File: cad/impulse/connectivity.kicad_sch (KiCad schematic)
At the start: 45 parts, among them J13 Micro_SD_Card, J14 Conn_Coaxial, U11 W25Q32JVSS, U12 BGS12PL6, U13 SX1268, Y2 XL7EL89COI-111YLC-32M

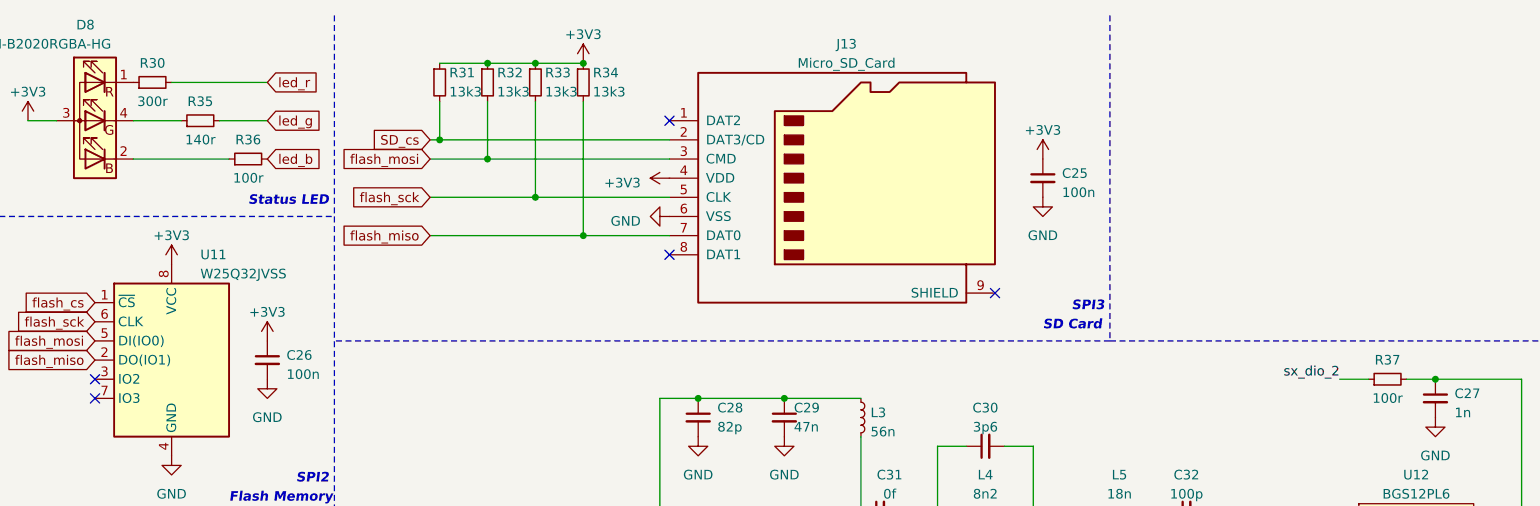
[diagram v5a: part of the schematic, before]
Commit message: Modified oscillator circuit.
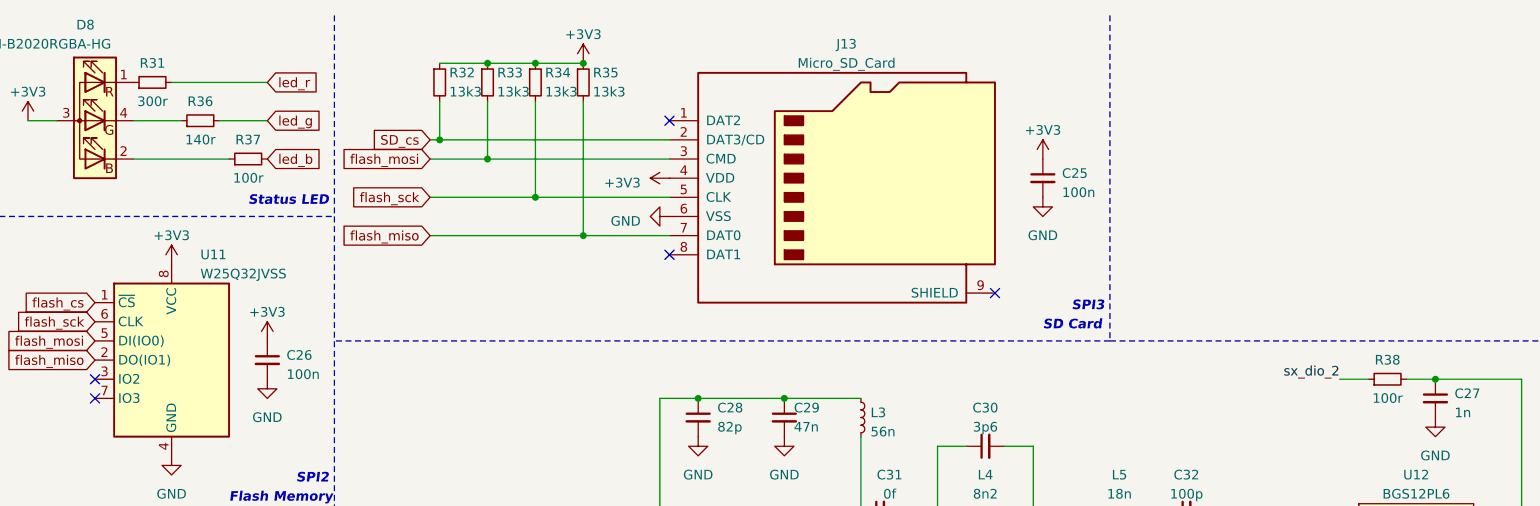
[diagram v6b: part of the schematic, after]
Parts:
- renumbered R30 to R31, R31 to R32, R32 to R33, R33 to R34, R34 to R35, R35 to R36, R36 to R37, R37 to R38
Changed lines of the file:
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@@
   (symbol (lib_id "Device:R_Small") (at 52.07 31.75 90) (unit 1)
     (in_bom yes) (on_board yes) (dnp no)
-    (property "Reference" "R36" (at 52.07 29.21 90)
+    (property "Reference" "R37" (at 52.07 29.21 90)
       (effects (font (size 1.27 1.27)))
     )
@@
       (project "impulse"
         (path "/eb4cfece-5fcb-437a-ac58-337ab6512039/b32decc0-dca7-4695-ab8c-927869a0cdf3"
-          (reference "R36") (unit 1)
+          (reference "R37") (unit 1)
         )
       )
@@
   (symbol (lib_id "Device:R_Small") (at 77.47 21.59 0) (unit 1)
     (in_bom yes) (on_board yes) (dnp no)
-    (property "Reference" "R31" (at 78.74 20.32 0)
+    (property "Reference" "R32" (at 78.74 20.32 0)
       (effects (font (size 1.27 1.27)) (justify left))
     )
@@
       (project "impulse"
         (path "/eb4cfece-5fcb-437a-ac58-337ab6512039/b32decc0-dca7-4695-ab8c-927869a0cdf3"
-          (reference "R31") (unit 1)
+          (reference "R32") (unit 1)
         )
       )
@@
   (symbol (lib_id "Device:R_Small") (at 45.72 26.67 90) (unit 1)
     (in_bom yes) (on_board yes) (dnp no)
-    (property "Reference" "R35" (at 45.72 24.13 90)
+    (property "Reference" "R36" (at 45.72 24.13 90)
       (effects (font (size 1.27 1.27)))
     )
@@
       (project "impulse"
         (path "/eb4cfece-5fcb-437a-ac58-337ab6512039/b32decc0-dca7-4695-ab8c-927869a0cdf3"
-          (reference "R35") (unit 1)
+          (reference "R36") (unit 1)
         )
       )
@@
   (symbol (lib_id "Device:R_Small") (at 203.2 60.96 90) (unit 1)
     (in_bom yes) (on_board yes) (dnp no)
-    (property "Reference" "R37" (at 203.2 58.42 90)
+    (property "Reference" "R38" (at 203.2 58.42 90)
       (effects (font (size 1.27 1.27)))
     )
@@
       (project "impulse"
         (path "/eb4cfece-5fcb-437a-ac58-337ab6512039/b32decc0-dca7-4695-ab8c-927869a0cdf3"
-          (reference "R37") (unit 1)
+          (reference "R38") (unit 1)
         )
       )
@@
   (symbol (lib_id "Device:R_Small") (at 90.17 21.59 0) (unit 1)
     (in_bom yes) (on_board yes) (dnp no)
-    (property "Reference" "R33" (at 91.44 20.32 0)
+    (property "Reference" "R34" (at 91.44 20.32 0)
       (effects (font (size 1.27 1.27)) (justify left))
     )
@@
       (project "impulse"
         (path "/eb4cfece-5fcb-437a-ac58-337ab6512039/b32decc0-dca7-4695-ab8c-927869a0cdf3"
+          (reference "R34") (unit 1)
+        )
+      )
+    )
+  )
+  (symbol (lib_id "Device:R_Small") (at 83.82 21.59 0) (unit 1)
+    (in_bom yes) (on_board yes) (dnp no)
+    (property "Reference" "R33" (at 85.09 20.32 0)
+      (effects (font (size 1.27 1.27)) (justify left))
+    )
+    (property "Value" "13k3" (at 85.09 22.86 0)
+      (effects (font (size 1.27 1.27)) (justify left))
+    )
+    (property "Footprint" "Resistor_SMD:R_0402_1005Metric" (at 83.82 21.59 0)
+      (effects (font (size 1.27 1.27)) hide)
+    )
+    (property "Datasheet" "~" (at 83.82 21.59 0)
+      (effects (font (size 1.27 1.27)) hide)
+    )
+    (property "lcsc" "C3015832" (at 83.82 21.59 0)
+      (effects (font (size 1.27 1.27)) hide)
+    )
+    (pin "1")
+    (pin "2")
+    (instances
+      (project "impulse"
+        (path "/eb4cfece-5fcb-437a-ac58-337ab6512039/b32decc0-dca7-4695-ab8c-927869a0cdf3"
           (reference "R33") (unit 1)
-        )
-      )
-    )
-  )
-  (symbol (lib_id "Device:R_Small") (at 83.82 21.59 0) (unit 1)
-    (in_bom yes) (on_board yes) (dnp no)
-    (property "Reference" "R32" (at 85.09 20.32 0)
-      (effects (font (size 1.27 1.27)) (justify left))
-    )
-    (property "Value" "13k3" (at 85.09 22.86 0)
-      (effects (font (size 1.27 1.27)) (justify left))
-    )
-    (property "Footprint" "Resistor_SMD:R_0402_1005Metric" (at 83.82 21.59 0)
-      (effects (font (size 1.27 1.27)) hide)
-    )
-    (property "Datasheet" "~" (at 83.82 21.59 0)
-      (effects (font (size 1.27 1.27)) hide)
-    )
-    (property "lcsc" "C3015832" (at 83.82 21.59 0)
-      (effects (font (size 1.27 1.27)) hide)
-    )
-    (pin "1")
-    (pin "2")
-    (instances
-      (project "impulse"
-        (path "/eb4cfece-5fcb-437a-ac58-337ab6512039/b32decc0-dca7-4695-ab8c-927869a0cdf3"
-          (reference "R32") (unit 1)
         )
       )
@@
   (symbol (lib_id "Device:R_Small") (at 96.52 21.59 0) (unit 1)
     (in_bom yes) (on_board yes) (dnp no)
-    (property "Reference" "R34" (at 97.79 20.32 0)
+    (property "Reference" "R35" (at 97.79 20.32 0)
       (effects (font (size 1.27 1.27)) (justify left))
     )
@@
       (project "impulse"
         (path "/eb4cfece-5fcb-437a-ac58-337ab6512039/b32decc0-dca7-4695-ab8c-927869a0cdf3"
-          (reference "R34") (unit 1)
+          (reference "R35") (unit 1)
         )
       )
@@
   (symbol (lib_id "Device:R_Small") (at 39.37 21.59 90) (unit 1)
     (in_bom yes) (on_board yes) (dnp no)
-    (property "Reference" "R30" (at 39.37 19.05 90)
+    (property "Reference" "R31" (at 39.37 19.05 90)
       (effects (font (size 1.27 1.27)))
     )
@@
       (project "impulse"
         (path "/eb4cfece-5fcb-437a-ac58-337ab6512039/b32decc0-dca7-4695-ab8c-927869a0cdf3"
-          (reference "R30") (unit 1)
-        )
-      )
+          (reference "R31") (unit 1)
+        )
+      )

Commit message: First layout.
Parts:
- renumbered R31 to R32, R32 to R33, R33 to R34, R34 to R35, R35 to R36, R36 to R37, R37 to R38, R38 to R39
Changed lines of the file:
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@@
   (symbol (lib_id "Device:R_Small") (at 52.07 31.75 90) (unit 1)
     (in_bom yes) (on_board yes) (dnp no)
-    (property "Reference" "R37" (at 52.07 29.21 90)
+    (property "Reference" "R38" (at 52.07 29.21 90)
       (effects (font (size 1.27 1.27)))
     )
@@
       (project "impulse"
         (path "/eb4cfece-5fcb-437a-ac58-337ab6512039/b32decc0-dca7-4695-ab8c-927869a0cdf3"
-          (reference "R37") (unit 1)
+          (reference "R38") (unit 1)
         )
       )
@@
   (symbol (lib_id "Device:R_Small") (at 77.47 21.59 0) (unit 1)
     (in_bom yes) (on_board yes) (dnp no)
-    (property "Reference" "R32" (at 78.74 20.32 0)
+    (property "Reference" "R33" (at 78.74 20.32 0)
       (effects (font (size 1.27 1.27)) (justify left))
     )
@@
       (project "impulse"
         (path "/eb4cfece-5fcb-437a-ac58-337ab6512039/b32decc0-dca7-4695-ab8c-927869a0cdf3"
-          (reference "R32") (unit 1)
+          (reference "R33") (unit 1)
         )
       )
@@
   (symbol (lib_id "Device:R_Small") (at 45.72 26.67 90) (unit 1)
     (in_bom yes) (on_board yes) (dnp no)
-    (property "Reference" "R36" (at 45.72 24.13 90)
+    (property "Reference" "R37" (at 45.72 24.13 90)
       (effects (font (size 1.27 1.27)))
     )
@@
       (project "impulse"
         (path "/eb4cfece-5fcb-437a-ac58-337ab6512039/b32decc0-dca7-4695-ab8c-927869a0cdf3"
-          (reference "R36") (unit 1)
+          (reference "R37") (unit 1)
         )
       )
@@
   (symbol (lib_id "Device:R_Small") (at 203.2 60.96 90) (unit 1)
     (in_bom yes) (on_board yes) (dnp no)
-    (property "Reference" "R38" (at 203.2 58.42 90)
+    (property "Reference" "R39" (at 203.2 58.42 90)
       (effects (font (size 1.27 1.27)))
     )
@@
       (project "impulse"
         (path "/eb4cfece-5fcb-437a-ac58-337ab6512039/b32decc0-dca7-4695-ab8c-927869a0cdf3"
-          (reference "R38") (unit 1)
+          (reference "R39") (unit 1)
         )
       )
@@
   (symbol (lib_id "Device:R_Small") (at 90.17 21.59 0) (unit 1)
     (in_bom yes) (on_board yes) (dnp no)
-    (property "Reference" "R34" (at 91.44 20.32 0)
+    (property "Reference" "R35" (at 91.44 20.32 0)
       (effects (font (size 1.27 1.27)) (justify left))
     )
@@
       (project "impulse"
         (path "/eb4cfece-5fcb-437a-ac58-337ab6512039/b32decc0-dca7-4695-ab8c-927869a0cdf3"
+          (reference "R35") (unit 1)
+        )
+      )
+    )
+  )
+  (symbol (lib_id "Device:R_Small") (at 83.82 21.59 0) (unit 1)
+    (in_bom yes) (on_board yes) (dnp no)
+    (property "Reference" "R34" (at 85.09 20.32 0)
+      (effects (font (size 1.27 1.27)) (justify left))
+    )
+    (property "Value" "13k3" (at 85.09 22.86 0)
+      (effects (font (size 1.27 1.27)) (justify left))
+    )
+    (property "Footprint" "Resistor_SMD:R_0402_1005Metric" (at 83.82 21.59 0)
+      (effects (font (size 1.27 1.27)) hide)
+    )
+    (property "Datasheet" "~" (at 83.82 21.59 0)
+      (effects (font (size 1.27 1.27)) hide)
+    )
+    (property "lcsc" "C3015832" (at 83.82 21.59 0)
+      (effects (font (size 1.27 1.27)) hide)
+    )
+    (pin "1")
+    (pin "2")
+    (instances
+      (project "impulse"
+        (path "/eb4cfece-5fcb-437a-ac58-337ab6512039/b32decc0-dca7-4695-ab8c-927869a0cdf3"
           (reference "R34") (unit 1)
-        )
-      )
-    )
-  )
-  (symbol (lib_id "Device:R_Small") (at 83.82 21.59 0) (unit 1)
-    (in_bom yes) (on_board yes) (dnp no)
-    (property "Reference" "R33" (at 85.09 20.32 0)
-      (effects (font (size 1.27 1.27)) (justify left))
-    )
-    (property "Value" "13k3" (at 85.09 22.86 0)
-      (effects (font (size 1.27 1.27)) (justify left))
-    )
-    (property "Footprint" "Resistor_SMD:R_0402_1005Metric" (at 83.82 21.59 0)
-      (effects (font (size 1.27 1.27)) hide)
-    )
-    (property "Datasheet" "~" (at 83.82 21.59 0)
-      (effects (font (size 1.27 1.27)) hide)
-    )
-    (property "lcsc" "C3015832" (at 83.82 21.59 0)
-      (effects (font (size 1.27 1.27)) hide)
-    )
-    (pin "1")
-    (pin "2")
-    (instances
-      (project "impulse"
-        (path "/eb4cfece-5fcb-437a-ac58-337ab6512039/b32decc0-dca7-4695-ab8c-927869a0cdf3"
-          (reference "R33") (unit 1)
         )
       )
@@
   (symbol (lib_id "Device:R_Small") (at 96.52 21.59 0) (unit 1)
     (in_bom yes) (on_board yes) (dnp no)
-    (property "Reference" "R35" (at 97.79 20.32 0)
+    (property "Reference" "R36" (at 97.79 20.32 0)
       (effects (font (size 1.27 1.27)) (justify left))
     )
@@
       (project "impulse"
         (path "/eb4cfece-5fcb-437a-ac58-337ab6512039/b32decc0-dca7-4695-ab8c-927869a0cdf3"
-          (reference "R35") (unit 1)
+          (reference "R36") (unit 1)
         )
       )
@@
   (symbol (lib_id "Device:R_Small") (at 39.37 21.59 90) (unit 1)
     (in_bom yes) (on_board yes) (dnp no)
-    (property "Reference" "R31" (at 39.37 19.05 90)
+    (property "Reference" "R32" (at 39.37 19.05 90)
       (effects (font (size 1.27 1.27)))
     )
@@
       (project "impulse"
         (path "/eb4cfece-5fcb-437a-ac58-337ab6512039/b32decc0-dca7-4695-ab8c-927869a0cdf3"
-          (reference "R31") (unit 1)
-        )
-      )
+          (reference "R32") (unit 1)
+        )
+      )

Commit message: Final version, ordered it.
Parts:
- C27: footprint Capacitor_SMD:C_0402_1005Metric -> Capacitor_SMD:C_0201_0603Metric; lcsc C53547 -> C301889
- C28: footprint Capacitor_SMD:C_0402_1005Metric -> Capacitor_SMD:C_0201_0603Metric; lcsc C525222 -> C285023
- C29: footprint Capacitor_SMD:C_0402_1005Metric -> Capacitor_SMD:C_0201_0603Metric; lcsc C5137574 -> C513424
- C30: footprint Capacitor_SMD:C_0402_1005Metric -> Capacitor_SMD:C_0201_0603Metric; lcsc C5186879 -> C525056
- C31, C38, C39, C43: footprint Capacitor_SMD:C_0402_1005Metric -> Capacitor_SMD:C_0201_0603Metric; lcsc (none) -> C3152011
- C32, C36: footprint Capacitor_SMD:C_0402_1005Metric -> Capacitor_SMD:C_0201_0603Metric; lcsc C1546 -> C5142539
- C33, C40: footprint Capacitor_SMD:C_0402_1005Metric -> Capacitor_SMD:C_0201_0603Metric; lcsc C482481 -> C525057
- C34: footprint Capacitor_SMD:C_0402_1005Metric -> Capacitor_SMD:C_0201_0603Metric; lcsc C1547 -> C50391
- C35: footprint Capacitor_SMD:C_0603_1608Metric -> Capacitor_SMD:C_0201_0603Metric; lcsc C5137629 -> C913427
- C41: footprint Capacitor_SMD:C_0402_1005Metric -> Capacitor_SMD:C_0201_0603Metric; lcsc C5137619 -> C285009
- C42: footprint Capacitor_SMD:C_0402_1005Metric -> Capacitor_SMD:C_0201_0603Metric; lcsc C696882 -> C285000
- L3: footprint Inductor_SMD:L_0402_1005Metric -> Inductor_SMD:L_0201_0603Metric; lcsc C90181 -> C963966
- L4: footprint Inductor_SMD:L_0402_1005Metric -> Inductor_SMD:L_0201_0603Metric; lcsc C90138 -> C2941401
- L5: footprint Inductor_SMD:L_0402_1005Metric -> Inductor_SMD:L_0201_0603Metric; lcsc C395050 -> C2913989
- L6: footprint Inductor_SMD:L_0402_1005Metric -> Inductor_SMD:L_0201_0603Metric; lcsc (none) -> C3152011
- L7: lcsc (none) -> C21376
- L8: footprint Inductor_SMD:L_0402_1005Metric -> Inductor_SMD:L_0201_0603Metric; lcsc C381885 -> C211337
